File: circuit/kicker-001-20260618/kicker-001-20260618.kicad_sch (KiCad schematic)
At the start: 64 parts, among them J1 Conn_Solenoid_{Front}, J2 Conn_Solenoid_{Back}, J3 Conn_Drribler_{Front}, J4 Conn_Relay, J5 Conn_Voltmeter, Q1 NMOS, Q2 PMOS, Q3 Q_Photo_CE, Q4 NMOS, Q5 NMOS, U1 74AHC1G04, U10 TLP2361, U11 74AHC1G08, U12 74AHC1G08, U2 TLP2361, U4 74AHC1G04, U5 74AHC1G04, U6 DRV8874, U7 74AHC1G04, U8 74AHC1G04, U9 TLP2361

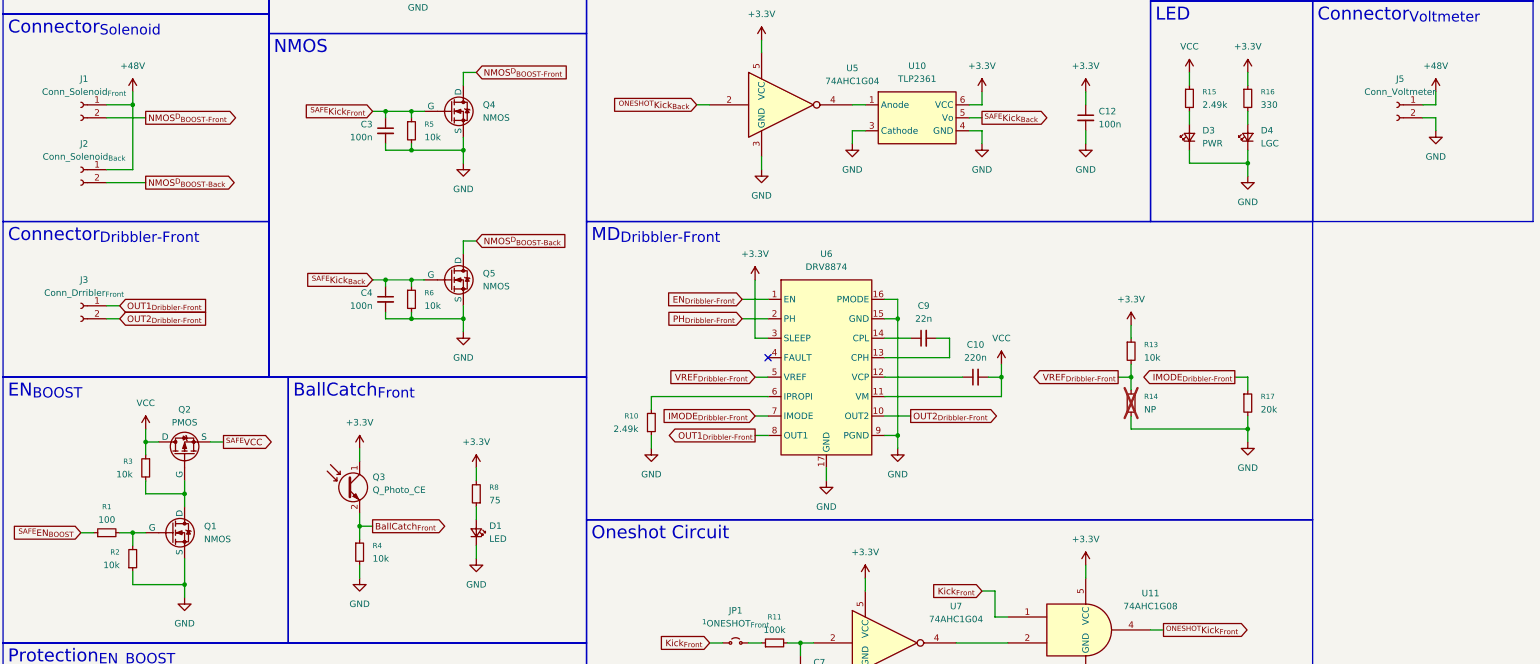
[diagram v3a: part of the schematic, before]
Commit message: Update キッカー基板の回路図を修正
・電圧計用のコネクタを3ピンに修正
・R2を10K→100Kに修正
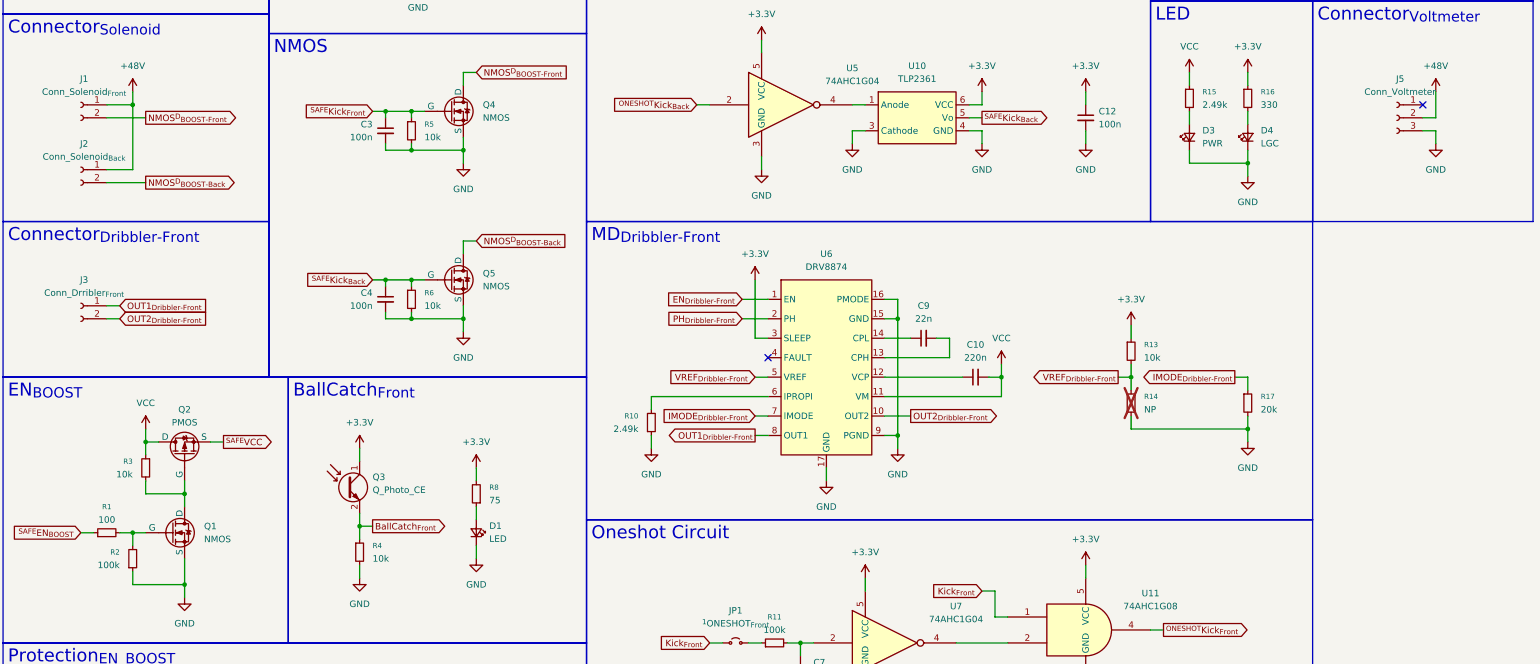
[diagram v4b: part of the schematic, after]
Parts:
- removed J5: Conn_Voltmeter, symbol Connector:Conn_01x02_Socket
- added J5: Conn_Voltmeter, symbol Connector:Conn_01x03_Socket
- R2: value 10k -> 100k
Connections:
- net +48V: now also J5.2 (Pin_2)
- net GND: now also J5.3 (Pin_3)
- no-connect marks 1 -> 2
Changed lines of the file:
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@@
 	)
 	(no_connect
+		(at 290.83 82.55)
+	)
+	(no_connect
 		(at 162.56 132.08)
 	)
@@
 	(wire
 		(pts
+			(xy 293.37 90.17) (xy 293.37 87.63)
+		)
+		(stroke
+			(width 0)
+			(type default)
+		)
+	)
+	(wire
+		(pts
 			(xy 44.45 38.1) (xy 41.91 38.1)
 		)
@@
 	(wire
 		(pts
-			(xy 293.37 80.01) (xy 293.37 82.55)
-		)
-		(stroke
-			(width 0)
-			(type default)
-		)
-	)
-	(wire
-		(pts
 			(xy 43.18 203.2) (xy 43.18 205.74)
 		)
@@
 	(wire
 		(pts
-			(xy 293.37 85.09) (xy 293.37 87.63)
-		)
-		(stroke
-			(width 0)
-			(type default)
-		)
-	)
-	(wire
-		(pts
 			(xy 87.63 91.44) (xy 87.63 90.17)
 		)
@@
 	(wire
 		(pts
+			(xy 293.37 87.63) (xy 290.83 87.63)
+		)
+		(stroke
+			(width 0)
+			(type default)
+		)
+	)
+	(wire
+		(pts
 			(xy 74.93 49.53) (xy 74.93 55.88)
 		)
@@
 	(wire
 		(pts
-			(xy 293.37 82.55) (xy 290.83 82.55)
-		)
-		(stroke
-			(width 0)
-			(type default)
-		)
-	)
-	(wire
-		(pts
 			(xy 185.42 128.27) (xy 190.5 128.27)
 		)
@@
 	(wire
 		(pts
+			(xy 293.37 80.01) (xy 293.37 85.09)
+		)
+		(stroke
+			(width 0)
+			(type default)
+		)
+	)
+	(wire
+		(pts
 			(xy 35.56 166.37) (xy 38.1 166.37)
 		)
@@
 	)
 	(symbol
+		(lib_id "Connector:Conn_01x03_Socket")
+		(at 285.75 85.09 0)
+		(mirror y)
+		(unit 1)
+		(body_style 1)
+		(exclude_from_sim no)
+		(in_bom yes)
+		(on_board yes)
+		(in_pos_files yes)
+		(dnp no)
+		(fields_autoplaced yes)
+		(property "Reference" "J5"
+			(at 286.385 77.47 0)
+			(show_name no)
+			(do_not_autoplace no)
+			(effects
+				(font
+					(size 1.27 1.27)
+				)
+			)
+		)
+		(property "Value" "Conn_Voltmeter"
+			(at 286.385 80.01 0)
+			(show_name no)
+			(do_not_autoplace no)
+			(effects
+				(font
+					(size 1.27 1.27)
+				)
+			)
+		)
+		(property "Footprint" ""
+			(at 285.75 85.09 0)
+			(hide yes)
+			(show_name no)
+			(do_not_autoplace no)
+			(effects
+				(font
+					(size 1.27 1.27)
+				)
+			)
+		)
+		(property "Datasheet" ""
+			(at 285.75 85.09 0)
+			(hide yes)
+			(show_name no)
+			(do_not_autoplace no)
+			(effects
+				(font
+					(size 1.27 1.27)
+				)
+			)
+		)
+		(property "Description" "Generic connector, single row, 01x03, script generated"
+			(at 285.75 85.09 0)
+			(hide yes)
+			(show_name no)
+			(do_not_autoplace no)
+			(effects
+				(font
+					(size 1.27 1.27)
+				)
+			)
+		)
+		(pin "3"
+		)
+		(pin "2"
+		)
+		(pin "1"
+		)
+		(instances
+			(project "kicker-001-20260618"
+				(path "/0c7db33d-45c2-4e7d-a877-ca4559957a30"
+					(reference "J5")
+					(unit 1)
+				)
+			)
+		)
+	)
+	(symbol
 		(lib_id "Device:C")
 		(at 280.67 38.1 0)
@@
 	(symbol
 		(lib_id "power:GND")
-		(at 293.37 87.63 0)
+		(at 293.37 90.17 0)
 		(unit 1)
 		(body_style 1)
@@
 		(fields_autoplaced yes)
 		(property "Reference" "#PWR060"
-			(at 293.37 93.98 0)
+			(at 293.37 96.52 0)
 			(hide yes)
 			(show_name no)
@@
 		)
 		(property "Value" "GND"
-			(at 293.37 92.71 0)
+			(at 293.37 95.25 0)
 			(show_name no)
 			(do_not_autoplace no)
@@
 		)
 		(property "Footprint" ""
-			(at 293.37 87.63 0)
+			(at 293.37 90.17 0)
 			(hide yes)
 			(show_name no)
@@
 		)
 		(property "Datasheet" ""
-			(at 293.37 87.63 0)
+			(at 293.37 90.17 0)
 			(hide yes)
 			(show_name no)
@@
 		)
 		(property "Description" "Power symbol creates a global label with name \"GND\" , ground"
-			(at 293.37 87.63 0)
+			(at 293.37 90.17 0)
 			(hide yes)
 			(show_name no)
@@
 	)
 	(symbol
-		(lib_id "Connector:Conn_01x02_Socket")
-		(at 285.75 82.55 0)
-		(mirror y)
-		(unit 1)
-		(body_style 1)
-		(exclude_from_sim no)
-		(in_bom yes)
-		(on_board yes)
-		(in_pos_files yes)
-		(dnp no)
-		(fields_autoplaced yes)
-		(property "Reference" "J5"
-			(at 286.385 77.47 0)
-			(show_name no)
-			(do_not_autoplace no)
-			(effects
-				(font
-					(size 1.27 1.27)
-				)
-			)
-		)
-		(property "Value" "Conn_Voltmeter"
-			(at 286.385 80.01 0)
-			(show_name no)
-			(do_not_autoplace no)
-			(effects
-				(font
-					(size 1.27 1.27)
-				)
-			)
-		)
-		(property "Footprint" ""
-			(at 285.75 82.55 0)
-			(hide yes)
-			(show_name no)
-			(do_not_autoplace no)
-			(effects
-				(font
-					(size 1.27 1.27)
-				)
-			)
-		)
-		(property "Datasheet" ""
-			(at 285.75 82.55 0)
-			(hide yes)
-			(show_name no)
-			(do_not_autoplace no)
-			(effects
-				(font
-					(size 1.27 1.27)
-				)
-			)
-		)
-		(property "Description" "Generic connector, single row, 01x02, script generated"
-			(at 285.75 82.55 0)
-			(hide yes)
-			(show_name no)
-			(do_not_autoplace no)
-			(effects
-				(font
-					(size 1.27 1.27)
-				)
-			)
-		)
-		(pin "1"
-		)
-		(pin "2"
-		)
-		(instances
-			(project "kicker-001-20260618"
-				(path "/0c7db33d-45c2-4e7d-a877-ca4559957a30"
-					(reference "J5")
-					(unit 1)
-				)
-			)
-		)
-	)
-	(symbol
 		(lib_id "power:GND")
 		(at 224.79 90.17 0)
@@
 			)
 		)
-		(property "Value" "10k"
+		(property "Value" "100k"
 			(at 35.56 172.7199 0)
 			(show_name no)

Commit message: Update キッカー基板のボード図を更新した
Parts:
- C1, C10, C11, C12, C2, C3, C4, C5, C6, C7, C8, C9: footprint (none) -> Capacitor_SMD:C_0603_1608Metric
- D1: footprint (none) -> LED_THT:LED_D3.0mm
- D3, D4: footprint (none) -> LED_SMD:LED_0603_1608Metric
- J1: value Conn_Solenoid_{Front} -> Conn_Solenoid_{Stroke}; footprint (none) -> Connector_JST:JST_XH_B2B-XH-A_1x02_P2.50mm_Vertical
- J2: value Conn_Solenoid_{Back} -> Conn_Solenoid_{Chip}; footprint (none) -> Connector_JST:JST_XH_B2B-XH-A_1x02_P2.50mm_Vertical
- J3: footprint (none) -> Connector_JST:JST_XH_B2B-XH-A_1x02_P2.50mm_Vertical
- J4: footprint (none) -> Connector_PinSocket_2.54mm:PinSocket_2x05_P2.54mm_Vertical
- J5: footprint (none) -> Connector_JST:JST_XH_B3B-XH-A_1x03_P2.50mm_Vertical
- JP1: value ^{1}ONESHOT_{Front} -> ^{1}ONESHOT_{Stroke}; footprint (none) -> Jumper:SolderJumper-2_P1.3mm_Open_RoundedPad1.0x1.5mm
- JP2: value ^{2}ONESHOT_{Front} -> ^{2}ONESHOT_{Stroke}; footprint (none) -> Jumper:SolderJumper-2_P1.3mm_Open_RoundedPad1.0x1.5mm
- JP3: value ^{1}ONESHOT_{Back} -> ^{1}ONESHOT_{Chip}; footprint (none) -> Jumper:SolderJumper-2_P1.3mm_Open_RoundedPad1.0x1.5mm
- JP4: value ^{2}ONESHOT_{Back} -> ^{2}ONESHOT_{Chip}; footprint (none) -> Jumper:SolderJumper-2_P1.3mm_Open_RoundedPad1.0x1.5mm
- R1, R10, R11, R12, R15, R16, R3, R4, R5, R6, R7, R8, R9: footprint (none) -> Resistor_SMD:R_0603_1608Metric
- R2: value 100k -> 10k; footprint (none) -> Resistor_SMD:R_0603_1608Metric
- U1, U11, U12, U4, U5, U7, U8: footprint (none) -> Package_TO_SOT_SMD:SOT-23-5_HandSoldering
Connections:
- net Kick_{Back} renamed Kick_{Chip}
- net Kick_{Front} renamed Kick_{Stroke}
- net NMOS^{D}_{BOOST-Back} renamed NMOS^{D}_{BOOST-Chip}
- net NMOS^{D}_{BOOST-Front} renamed NMOS^{D}_{BOOST-Stroke}
- net ^{ONESHOT}Kick_{Back} renamed ^{ONESHOT}Kick_{Chip}
- net ^{ONESHOT}Kick_{Front} renamed ^{ONESHOT}Kick_{Stroke}
- net ^{SAFE}Kick_{Back} renamed ^{SAFE}Kick_{Chip}
- net ^{SAFE}Kick_{Front} renamed ^{SAFE}Kick_{Stroke}

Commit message: Update キッカー基板のフットプリント紐づけをやった
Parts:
- C13, C14, C15, C16: footprint (none) -> Capacitor_THT:C_Radial_D12.5mm_H25.0mm_P5.00mm
- Q1: value NMOS -> BSS138; footprint (none) -> Package_TO_SOT_SMD:TSOT-23
- Q2: value PMOS -> TJ15S06M3L; footprint (none) -> Package_TO_SOT_SMD:TO-252-2
- Q4, Q5: value NMOS -> MTB010N06RJ3; footprint (none) -> Package_TO_SOT_SMD:TO-252-2
- U6: footprint (none) -> Package_SO:HTSSOP-16-1EP_4.4x5mm_P0.65mm_EP3.4x5mm_Mask2.66x2.46mm
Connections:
- net GND: now also Q1.2 (S); no longer Q1.3 (S)
- net NMOS^{D}_{BOOST-Chip}: now also Q5.2 (D); no longer Q5.1 (D)
- net NMOS^{D}_{BOOST-Stroke}: now also Q4.2 (D); no longer Q4.1 (D)
- net VCC: now also Q2.2 (D); no longer Q2.1 (D)
- net ^{SAFE}Kick_{Chip}: now also Q5.1 (G); no longer Q5.2 (G)
- net ^{SAFE}Kick_{Stroke}: now also Q4.1 (G); no longer Q4.2 (G)
- net at R1.2, R2.2: now also Q1.1 (G); no longer Q1.2 (G)
- new net: Q1.3 (D), Q2.1 (G), R3.2
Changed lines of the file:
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@@
 		)
 	)
+	(text_box "MOSFETのシンボルとフットプリントの連携をする際\n必ずDS上のMechanicalなPinAssignとSymbolのPinAssignが\n対応しているかを確認すること、しないと燃える！"
+		(exclude_from_sim no)
+		(at 12.7 238.76 0)
+		(size 114.3 30.48)
+		(margins 0.9525 0.9525 0.9525 0.9525)
+		(stroke
+			(width 0)
+			(type solid)
+		)
+		(fill
+			(type none)
+		)
+		(effects
+			(font
+				(face "游ゴシック")
+				(size 2.54 2.54)
+				(thickness 0.508)
+				(bold yes)
+			)
+			(justify left)
+		)
+	)
 	(text_box "LED"
 		(exclude_from_sim no)
@@
 			)
 		)
-		(property "Footprint" ""
+		(property "Footprint" "Package_SO:HTSSOP-16-1EP_4.4x5mm_P0.65mm_EP3.4x5mm_Mask2.66x2.46mm"
 			(at 173.99 111.76 0)
 			(hide yes)
@@
 	)
 	(symbol
+		(lib_name "NMOS_2")
 		(lib_id "Simulation_SPICE:NMOS")
 		(at 100.33 116.84 0)
@@
 			)
 		)
-		(property "Value" "NMOS"
+		(property "Value" "MTB010N06RJ3"
 			(at 106.68 118.1099 0)
 			(show_name no)
@@
 			)
 		)
-		(property "Footprint" ""
+		(property "Footprint" "Package_TO_SOT_SMD:TO-252-2"
 			(at 105.41 114.3 0)
 			(hide yes)
@@
 			)
 		)
-		(property "Footprint" ""
+		(property "Footprint" "Capacitor_THT:C_Radial_D12.5mm_H25.0mm_P5.00mm"
 			(at 281.6352 41.91 0)
 			(hide yes)
@@
 			)
 		)
-		(property "Footprint" ""
+		(property "Footprint" "Capacitor_THT:C_Radial_D12.5mm_H25.0mm_P5.00mm"
 			(at 296.8752 41.91 0)
 			(hide yes)
@@
 	)
 	(symbol
+		(lib_name "NMOS_1")
 		(lib_id "Simulation_SPICE:NMOS")
 		(at 100.33 83.82 0)
@@
 			)
 		)
-		(property "Value" "NMOS"
+		(property "Value" "MTB010N06RJ3"
 			(at 106.68 85.0899 0)
 			(show_name no)
@@
 			)
 		)
-		(property "Footprint" ""
+		(property "Footprint" "Package_TO_SOT_SMD:TO-252-2"
 			(at 105.41 81.28 0)
 			(hide yes)
@@
 			)
 		)
-		(property "Value" "PMOS"
+		(property "Value" "TJ15S06M3L"
 			(at 48.26 144.78 90)
 			(show_name no)
@@
 			)
 		)
-		(property "Footprint" ""
+		(property "Footprint" "Package_TO_SOT_SMD:TO-252-2"
 			(at 45.72 146.05 0)
 			(hide yes)
@@
 			)
 		)
-		(property "Footprint" ""
+		(property "Footprint" "Capacitor_THT:C_Radial_D12.5mm_H25.0mm_P5.00mm"
 			(at 266.3952 41.91 0)
 			(hide yes)
@@
 			)
 		)
-		(property "Value" "NMOS"
+		(property "Value" "BSS138"
 			(at 52.07 167.6399 0)
 			(show_name no)
@@
 			)
 		)
-		(property "Footprint" ""
+		(property "Footprint" "Package_TO_SOT_SMD:TSOT-23"
 			(at 50.8 163.83 0)
 			(hide yes)
@@
 			)
 		)
-		(property "Footprint" ""
+		(property "Footprint" "Capacitor_THT:C_Radial_D12.5mm_H25.0mm_P5.00mm"
 			(at 251.1552 41.91 0)
 			(hide yes)

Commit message: Update キッカー基板のcommit残り
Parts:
- removed J4: Conn_Relay, Connector_PinSocket_2.54mm:PinSocket_2x05_P2.54mm_Vertical, symbol Connector_Generic:Conn_02x05_Counter_Clockwise
- added J4: Conn_Relay, Connector_PinSocket_2.54mm:PinSocket_2x05_P2.54mm_Vertical, symbol Connector_Generic:Conn_02x05_Odd_Even
- C1: value 47u -> 47μ
- C13, C14, C15, C16: value 1000u -> 1000μ
- C2, C6: value 1u -> 1μ
- C7, C8: value 10u -> 10μ
- D2: value D_Small -> CUHS20F60; footprint (none) -> @Thrive_footprint_kicker:CUHS20F60
- J1: value Conn_Solenoid_{Stroke} -> Solenoid_{Stroke}
- J2: value Conn_Solenoid_{Chip} -> Solenoid_{Chip}
- J3: value Conn_Drribler_{Front} -> Drribler_{Front}
- J5: value Conn_Voltmeter -> Voltmeter
- JP1: value ^{1}ONESHOT_{Stroke} -> Stroke_{OS-ON}
- JP2: value ^{2}ONESHOT_{Stroke} -> Stroke_{OS-OFF}
- JP3: value ^{1}ONESHOT_{Chip} -> Chip_{OS-ON}
- JP4: value ^{2}ONESHOT_{Chip} -> Chip_{OS-OFF}
- Q3: footprint (none) -> @Thrive_footprint_kicker:NJL7502L
- U3: value (none) -> XL6009E1
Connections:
- net +3.3V: now also J4.10 (Pin_10)
- net +48V: now also J2.2 (Pin_2); no longer J2.1 (Pin_1)
- net BallCatch_{Front}: now also J4.7 (Pin_7)
- net EN_{BOOST}: now also J4.2 (Pin_2)
- net EN_{Dribbler-Front}: now also J4.3 (Pin_3)
- net GND: now also D1.2 (K), J4.1 (Pin_1), J4.9 (Pin_9); no longer D1.1 (K)
- net Kick_{Chip}: now also J4.4 (Pin_4)
- net Kick_{Stroke}: now also J4.8 (Pin_8)
- net NMOS^{D}_{BOOST-Chip}: now also J2.1 (Pin_1); no longer J2.2 (Pin_2)
- net OUT1_{Dribbler-Front}: now also J3.2 (Pin_2); no longer J3.1 (Pin_1)
- net OUT2_{Dribbler-Front}: now also J3.1 (Pin_1); no longer J3.2 (Pin_2)
- net PH_{Dribbler-Front}: now also J4.5 (Pin_5)
- net VCC: now also J4.6 (Pin_6)
- net at R8.1: now also D1.1 (A); no longer D1.2 (A)
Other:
- moved on the sheet: C10, C12, C7, C8, C9, D3, D4, JP1, JP2, JP3, JP4, R10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

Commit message: Update キッカー基板のボード図完成
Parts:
- removed J5: Voltmeter, Connector_JST:JST_XH_B3B-XH-A_1x03_P2.50mm_Vertical, symbol Connector:Conn_01x03_Socket
- added J6: Voltmeter, Connector_JST:JST_XH_B2B-XH-A_1x02_P2.50mm_Vertical, symbol Connector:Conn_01x02_Socket
- JP1: value Stroke_{OS-ON} -> _{ON}
- JP2: value Stroke_{OS-OFF} -> _{OFF}
- JP3: value Chip_{OS-ON} -> _{ON}
- JP4: value Chip_{OS-OFF} -> _{OFF}
- L1: footprint (none) -> @Thrive_footprint_kicker:SRC1317
- U1, U4, U5, U7, U8: value 74AHC1G04 -> NOT
- U11, U12: value 74AHC1G08 -> AND
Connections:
- net +48V: now also J6.1 (Pin_1)
- net GND: now also J6.2 (Pin_2)
- no-connect marks 2 -> 1
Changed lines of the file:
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@@
 	)
 	(no_connect
-		(at 290.83 82.55)
-	)
-	(no_connect
 		(at 162.56 130.81)
 	)
@@
 			)
 		)
-		(property "Value" "74AHC1G08"
+		(property "Value" "AND"
 			(at 237.49 221.4151 0)
 			(show_name no)
@@
 			)
 		)
-		(property "Footprint" ""
+		(property "Footprint" "@Thrive_footprint_kicker:SRC1317"
 			(at 93.98 34.29 0)
 			(hide yes)
@@
 			)
 		)
-		(property "Value" "74AHC1G08"
+		(property "Value" "AND"
 			(at 237.49 179.5051 0)
 			(show_name no)
@@
 	)
 	(symbol
-		(lib_id "Connector:Conn_01x03_Socket")
-		(at 285.75 85.09 0)
-		(mirror y)
-		(unit 1)
-		(body_style 1)
-		(exclude_from_sim no)
-		(in_bom yes)
-		(on_board yes)
-		(in_pos_files yes)
-		(dnp no)
-		(fields_autoplaced yes)
-		(property "Reference" "J5"
-			(at 286.385 77.47 0)
-			(show_name no)
-			(do_not_autoplace no)
-			(effects
-				(font
-					(size 1.27 1.27)
-				)
-			)
-		)
-		(property "Value" "Voltmeter"
-			(at 286.385 80.01 0)
-			(show_name no)
-			(do_not_autoplace no)
-			(effects
-				(font
-					(size 1.27 1.27)
-				)
-			)
-		)
-		(property "Footprint" "Connector_JST:JST_XH_B3B-XH-A_1x03_P2.50mm_Vertical"
-			(at 285.75 85.09 0)
-			(hide yes)
-			(show_name no)
-			(do_not_autoplace no)
-			(effects
-				(font
-					(size 1.27 1.27)
-				)
-			)
-		)
-		(property "Datasheet" ""
-			(at 285.75 85.09 0)
-			(hide yes)
-			(show_name no)
-			(do_not_autoplace no)
-			(effects
-				(font
-					(size 1.27 1.27)
-				)
-			)
-		)
-		(property "Description" "Generic connector, single row, 01x03, script generated"
-			(at 285.75 85.09 0)
-			(hide yes)
-			(show_name no)
-			(do_not_autoplace no)
-			(effects
-				(font
-					(size 1.27 1.27)
-				)
-			)
-		)
-		(pin "3"
-		)
-		(pin "2"
-		)
-		(pin "1"
-		)
-		(instances
-			(project "kicker-001-20260618"
-				(path "/0c7db33d-45c2-4e7d-a877-ca4559957a30"
-					(reference "J5")
-					(unit 1)
-				)
-			)
-		)
-	)
-	(symbol
 		(lib_id "Device:C")
 		(at 280.67 38.1 0)
@@
 			)
 		)
-		(property "Value" "Stroke_{OS-ON}"
+		(property "Value" "_{ON}"
 			(at 156.21 182.88 0)
 			(show_name no)
@@
 			)
 		)
-		(property "Value" "74AHC1G04"
+		(property "Value" "NOT"
 			(at 199.39 182.0451 0)
 			(show_name no)
@@
 			)
 		)
-		(property "Value" "74AHC1G04"
+		(property "Value" "NOT"
 			(at 179.07 74.0951 0)
 			(show_name no)
@@
 			)
 		)
-		(property "Value" "Chip_{OS-ON}"
+		(property "Value" "_{ON}"
 			(at 156.21 224.79 0)
 			(show_name no)
@@
 			)
 		)
-		(property "Value" "74AHC1G04"
+		(property "Value" "NOT"
 			(at 60.96 211.2551 0)
 			(show_name no)
@@
 			)
 		)
-		(property "Value" "74AHC1G04"
+		(property "Value" "NOT"
 			(at 199.39 223.9551 0)
 			(show_name no)
@@
 			)
 		)
-		(property "Value" "Stroke_{OS-OFF}"
+		(property "Value" "_{OFF}"
 			(at 156.21 205.74 0)
 			(show_name no)
@@
 			)
 		)
-		(property "Value" "74AHC1G04"
+		(property "Value" "NOT"
 			(at 179.07 33.4551 0)
 			(show_name no)
@@
 			)
 		)
-		(property "Value" "Chip_{OS-OFF}"
+		(property "Value" "_{OFF}"
 			(at 156.21 247.65 0)
 			(show_name no)
@@
 					(unit 1)
 				)
+			)
+		)
+	)
+	(symbol
+		(lib_id "Connector:Conn_01x02_Socket")
+		(at 285.75 85.09 0)
+		(mirror y)
+		(unit 1)
+		(body_style 1)
+		(exclude_from_sim no)
+		(in_bom yes)
+		(on_board yes)
+		(in_pos_files yes)
+		(dnp no)
+		(fields_autoplaced yes)
+		(property "Reference" "J6"
+			(at 286.385 80.01 0)
+			(show_name no)
+			(do_not_autoplace no)
+			(effects
+				(font
+					(size 1.27 1.27)
+				)
+			)
+		)
+		(property "Value" "Voltmeter"
+			(at 286.385 82.55 0)
+			(show_name no)
+			(do_not_autoplace no)
+			(effects
+				(font
+					(size 1.27 1.27)
+				)
+			)
+		)
+		(property "Footprint" "Connector_JST:JST_XH_B2B-XH-A_1x02_P2.50mm_Vertical"
+			(at 285.75 85.09 0)
+			(hide yes)
+			(show_name no)
+			(do_not_autoplace no)
+			(effects
+				(font
+					(size 1.27 1.27)
+				)
+			)
+		)
+		(property "Datasheet" ""
+			(at 285.75 85.09 0)
+			(hide yes)
+			(show_name no)
+			(do_not_autoplace no)
+			(effects
+				(font
+					(size 1.27 1.27)
+				)
+			)
+		)
+		(property "Description" "Generic connector, single row, 01x02, script generated"
+			(at 285.75 85.09 0)
+			(hide yes)
+			(show_name no)
+			(do_not_autoplace no)
+			(effects
+				(font
+					(size 1.27 1.27)
+				)
+			)
+		)
+		(pin "2"
+		)
+		(pin "1"
+		)
+		(instances
+			(project "kicker-001-20260618"
+				(path "/0c7db33d-45c2-4e7d-a877-ca4559957a30"
+					(reference "J6")
+					(unit 1)
+				)
